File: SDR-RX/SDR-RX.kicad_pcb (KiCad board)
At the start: 2 copper layers, 53 x 51 mm, 49 parts, among them J1 Program, J2 Vin, J3 FM Antenna, J4 AM Antenna, J5 Conn_01x03_Male, J6 GPS, Q1 S8050, Q2 S8050, SW1 Reset ESP, SW2 3V3 J5/J2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

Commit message: changed footprint GPS header
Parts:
- removed J1: Program, Connector_JST:JST_XH_S7B-XH-A-1_1x07_P2.50mm_Horizontal
- removed J2: Vin, Connector_JST:JST_XH_B2B-XH-A_1x02_P2.50mm_Vertical
- removed J3: FM Antenna, Connector_Coaxial:SMA_Samtec_SMA-J-P-X-ST-EM1_EdgeMount
- removed J5: Conn_01x03_Male, Connector_PinHeader_2.54mm:PinHeader_1x03_P2.54mm_Vertical
- removed J6: GPS, Connector_JST:JST_SH_BM04B-SRSS-TB_1x04-1MP_P1.00mm_Vertical
- removed SW1: Reset ESP, Button_Switch_SMD:SW_SPST_B3SL-1002P
- removed SW2: 3V3 J5/J2, Button_Switch_SMD:SW_SPDT_CK-JS102011SAQN
- removed TP1: Reset ESP, TestPoint:TestPoint_Pad_D1.5mm
- removed TP2: Data, TestPoint:TestPoint_Pad_D1.5mm
- removed TP3: Clock, TestPoint:TestPoint_Pad_D1.5mm
- removed TP4: Reset SI4734, TestPoint:TestPoint_Pad_D1.5mm
- removed TP5: TestPoint, TestPoint:TestPoint_Pad_D1.5mm
- added +3V3: TP5, TestPoint:TestPoint_Pad_D1.5mm, F.Cu at (425.9, 86.4)
- added Clock: Clock, TestPoint:TestPoint_Pad_D1.5mm, F.Cu at (420.9, 86.4)
- added Data: Data, TestPoint:TestPoint_Pad_D1.5mm, F.Cu at (425.9, 81.3)
- added FM Antenna: J3, Connector_Coaxial:SMA_Samtec_SMA-J-P-X-ST-EM1_EdgeMount, F.Cu at (428.5, 56.9)
- added GND: Conn_01x03_Male, Connector_PinHeader_2.54mm:PinHeader_1x03_P2.54mm_Vertical, F.Cu at (409.4, 92.8)
- added GPS: J6, Connector_JST:JST_SH_BM04B-SRSS-TB_1x04-1MP_P1.00mm_Vertical, F.Cu at (419.6, 52.1)
- added Program: J1, Connector_JST:JST_XH_S7B-XH-A-1_1x07_P2.50mm_Horizontal, F.Cu at (380.2, 55.9)
- added Reset ESP: Reset ESP, TestPoint:TestPoint_Pad_D1.5mm, F.Cu at (420.9, 91.5)
- added Reset ESP: SW1, Button_Switch_SMD:SW_SPST_B3SL-1002P, F.Cu at (409.4, 85.1)
- added Reset SI4734: Reset SI4734, TestPoint:TestPoint_Pad_D1.5mm, F.Cu at (425.9, 76.2)
- added Vin : J2, Connector_JST:JST_XH_B2B-XH-A_1x02_P2.50mm_Vertical, F.Cu at (389.1, 92.8)
- added sel. 3V3 : SW2, Button_Switch_SMD:SW_SPDT_CK-JS102011SAQN, F.Cu at (380.2, 80.1)
- moved C11 255.2 mm to (412.0, 71.2)
- moved C2 255.2 mm to (419.6, 80.5)
- moved C3 255.2 mm to (427.2, 72.4)
- moved C8 255.2 mm to (423.4, 59.7)
- moved D3 255.2 mm to (412.0, 75.0)
- moved FB1 255.2 mm to (387.9, 87.7)
- moved Q1 255.2 mm to (412.0, 78.8)
- moved R1 255.2 mm to (412.0, 68.6)
- moved U1 255.2 mm to (419.6, 71.2)
- moved C1 255.2 mm to (417.1, 80.4)
- moved C10 255.2 mm to (428.5, 62.3)
- moved C12 255.2 mm to (381.5, 87.7)
- moved C13 255.2 mm to (394.2, 87.7)
- moved C4 255.2 mm to (420.9, 59.7)
- moved C5 255.2 mm to (389.1, 73.3)
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
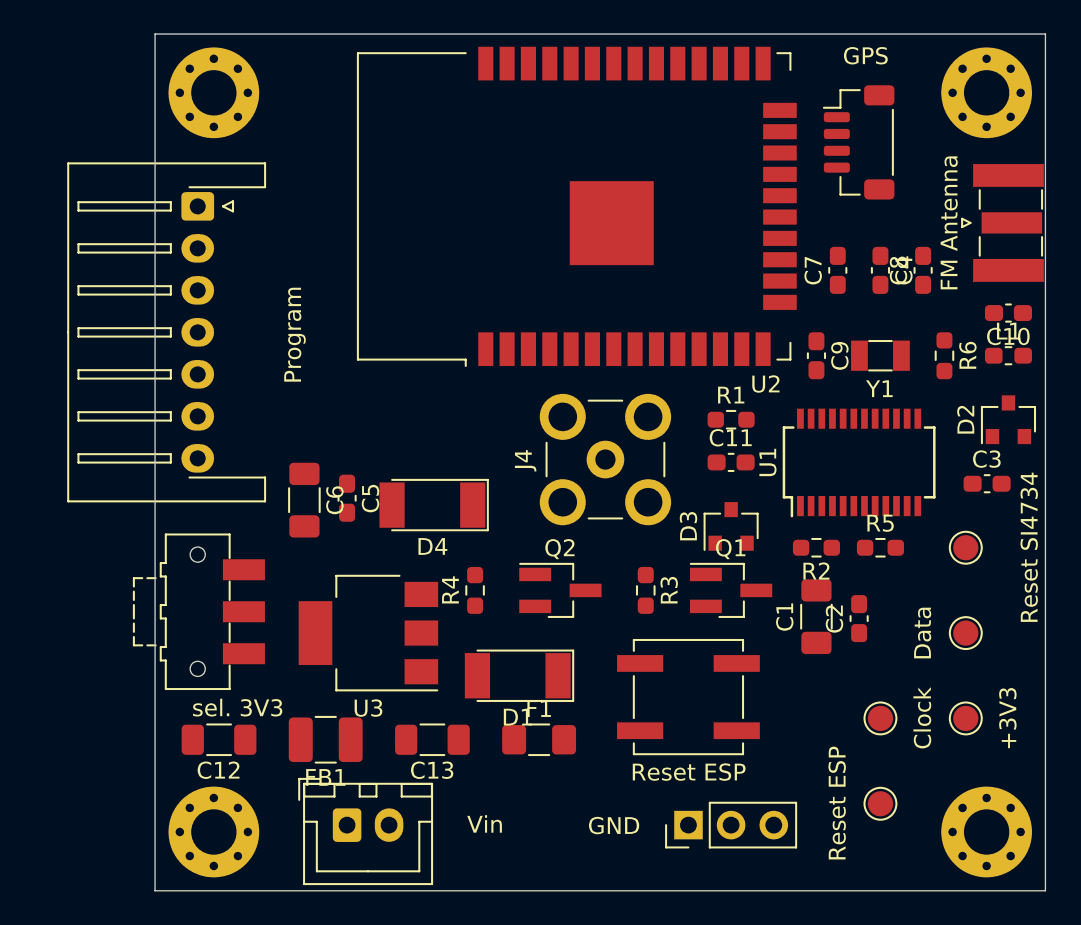
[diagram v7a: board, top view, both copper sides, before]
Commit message: round corners
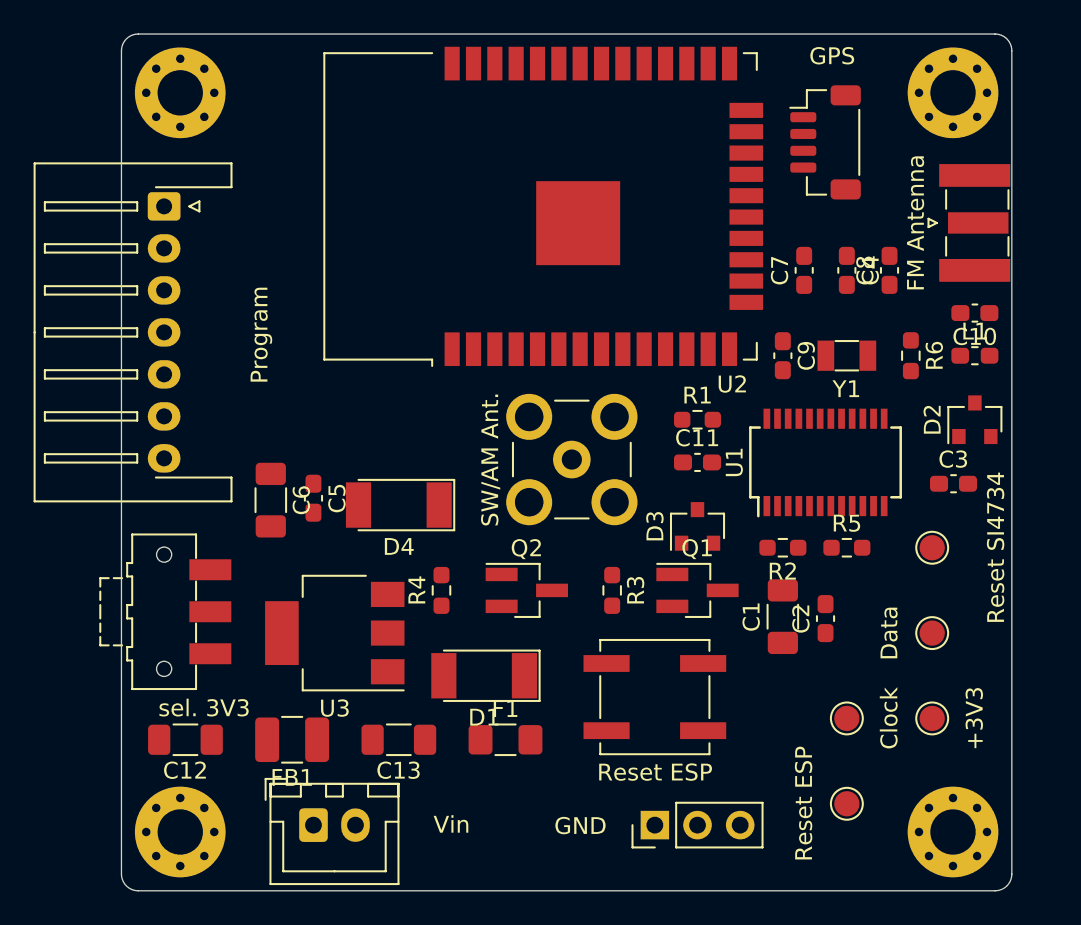
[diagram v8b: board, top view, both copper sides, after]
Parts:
- SW/AM Ant.: renamed from J4
- moved +3V3 2.00 mm to (423.9, 86.4)
- moved C1 2.00 mm to (415.1, 80.4)
- moved C10 2.00 mm to (426.5, 62.3)
- moved C11 2.00 mm to (410.0, 71.2)
- moved C12 2.00 mm to (379.5, 87.7)
- moved C13 2.00 mm to (392.2, 87.7)
- moved C2 2.00 mm to (417.6, 80.5)
- moved C3 2.00 mm to (425.2, 72.4)
- moved C4 2.00 mm to (418.9, 59.7)
- moved C5 2.00 mm to (387.1, 73.3)
- moved C6 2.00 mm to (384.6, 73.4)
- moved C7 2.00 mm to (416.3, 59.7)
- moved C8 2.00 mm to (421.4, 59.7)
- moved C9 2.00 mm to (415.1, 64.8)
- moved Clock 2.00 mm to (418.9, 86.4)
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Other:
- outline, holes or cut-outs redrawn
